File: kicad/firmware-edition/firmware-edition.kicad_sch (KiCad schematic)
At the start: 109 parts, among them J1 Solar Panel, J10 GPIO, J11 I2C-3V3, J12 GPIO, J13 SPI, J14 I2C-5V, J15 SWD, J16 Conn_01x01_Pin, J17 Conn_01x01_Pin, J18 Conn_01x01_Pin, J19 Conn_01x01_Pin, J2 BATT, J20 Conn_01x01_Pin, J21 GPIO, J3 3V3 Sensor Bus, J4 USB_C_Receptacle_USB2.0_16P, J5 Conn_01x01_Pin, J6 Conn_01x01_Pin, J7 Conn_01x01_Socket, J8 GPIO, J9 Conn_01x01_Pin, Q1 BSS84, Q2 BSS84, Q3 BSS84, SW1 BOOT_DFU, SW2 RST, U1 ADP5091, U2 TPS61023DRLR, U3 MAX-M10M-00B, U4 Si4463, U5 STM32U073KCU6, U6 TXS0102VDCTR, Y1 30MHz

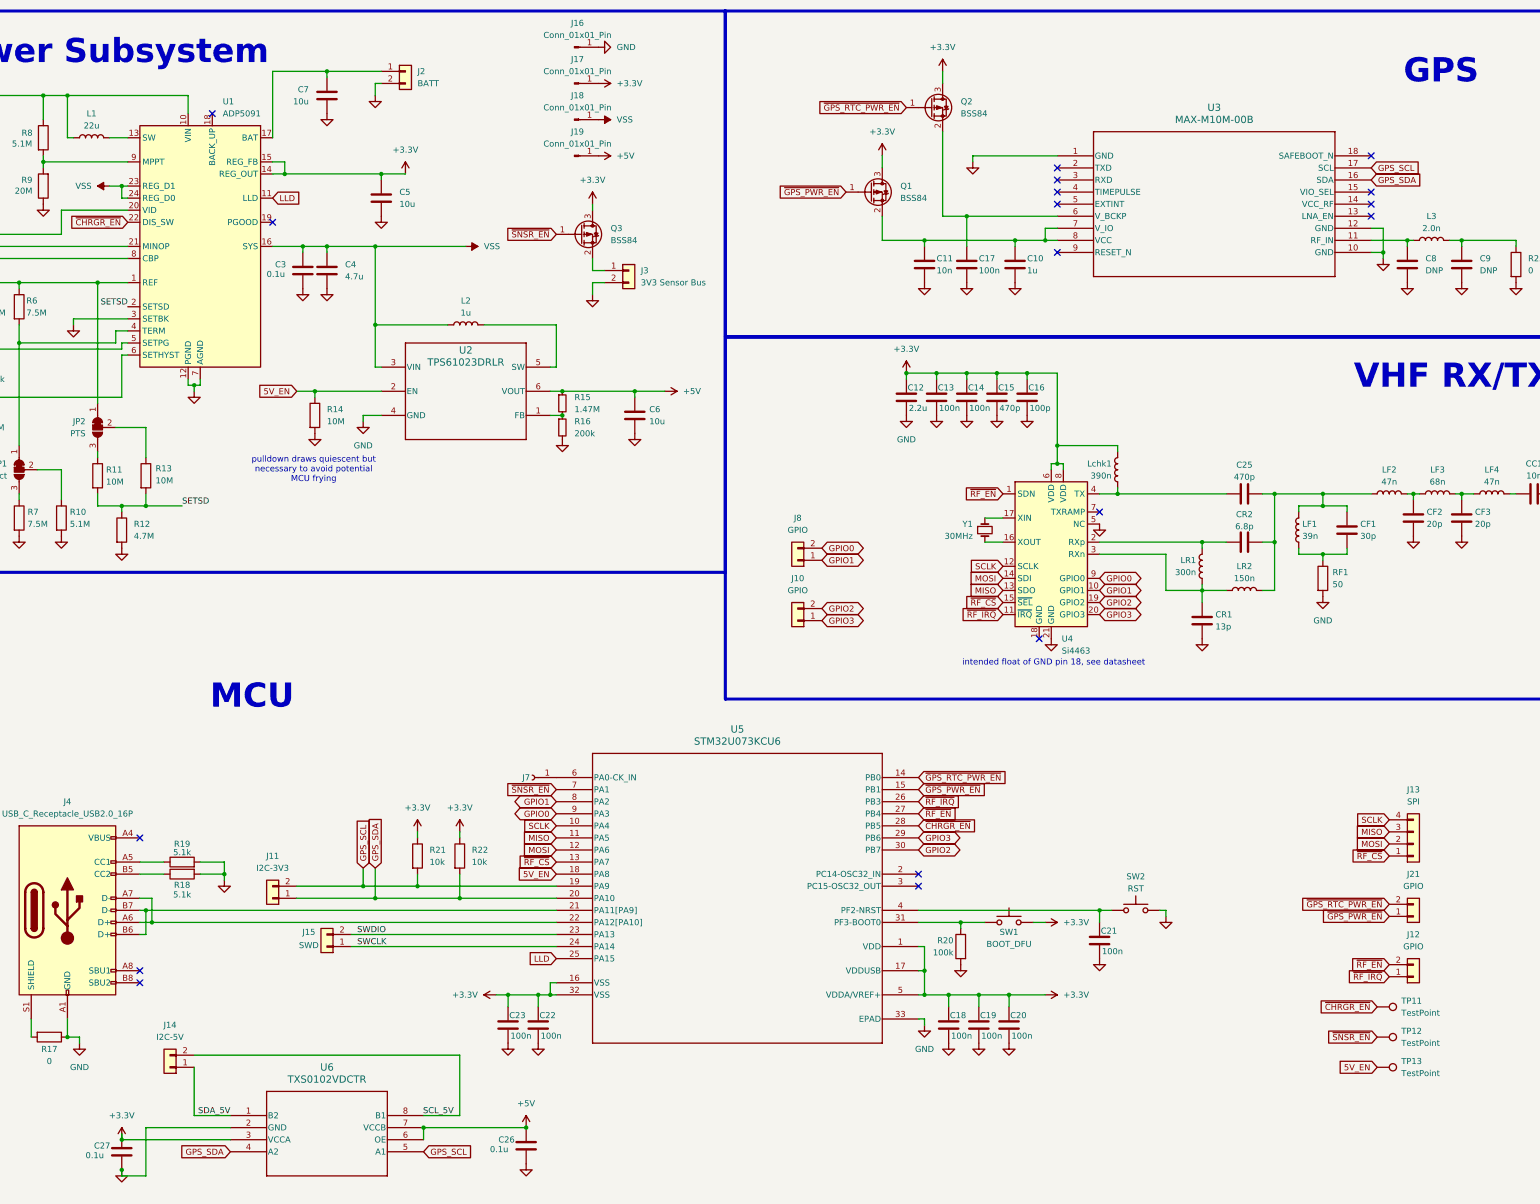
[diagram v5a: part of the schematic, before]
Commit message: improved layout, added PGOOD to MCU connection
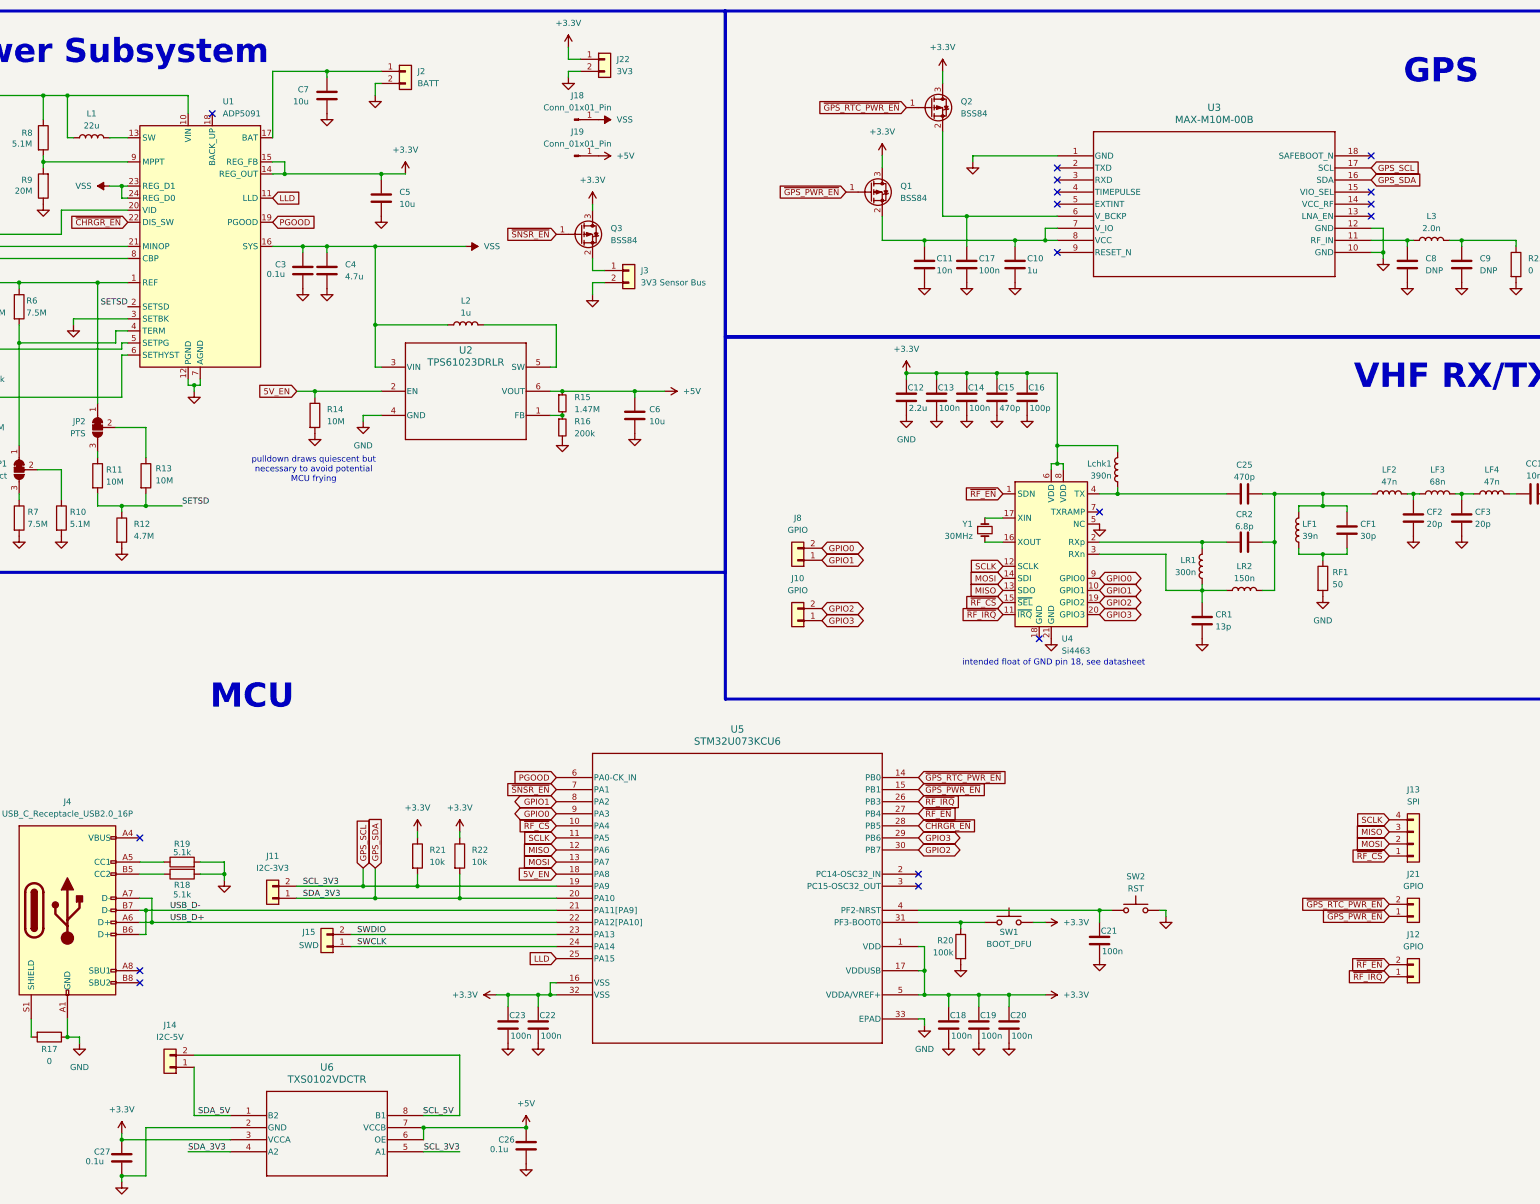
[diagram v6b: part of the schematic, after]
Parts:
- removed J16: Conn_01x01_Pin, Connector_PinHeader_2.54mm:PinHeader_1x02_P2.54mm_Vertical, symbol Connector:Conn_01x01_Pin
- removed J17: Conn_01x01_Pin, Connector_PinHeader_2.54mm:PinHeader_1x01_P2.54mm_Vertical, symbol Connector:Conn_01x01_Pin
- removed J7: Conn_01x01_Socket, Connector_PinHeader_1.00mm:PinHeader_1x01_P1.00mm_Vertical, symbol Connector:Conn_01x01_Socket
- removed TP11, TP12, TP13: TestPoint, Connector_PinHeader_1.00mm:PinHeader_1x01_P1.00mm_Vertical, symbol Connector:TestPoint
- added J22: 3V3, Connector_PinSocket_2.54mm:PinSocket_1x02_P2.54mm_Vertical, symbol Connector_Generic:Conn_01x02
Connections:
- net +3.3V: now also J22.1 (Pin_1)
- net GND: now also J22.2 (Pin_2)
- net MISO: now also U5.12 (PA6); no longer U5.11 (PA5)
- net MOSI: now also U5.13 (PA7); no longer U5.12 (PA6)
- net SCLK: now also U5.11 (PA5); no longer U5.10 (PA4)
- net ~{RF_CS}: now also U5.10 (PA4); no longer U5.13 (PA7)
- net USB_D+: now reaches J4.A6 (D+), J4.A7 (D-), U5.22 (PA12[PA10])
- net USB_D-: now reaches J4.B6 (D+), J4.B7 (D-), U5.21 (PA11[PA9])
- net PGOOD: now reaches U1.19 (PGOOD)
- net PGOOD: now also U5.6 (PA0-CK_IN)
- no-connect marks 18 -> 17
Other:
- moved on the sheet: C27

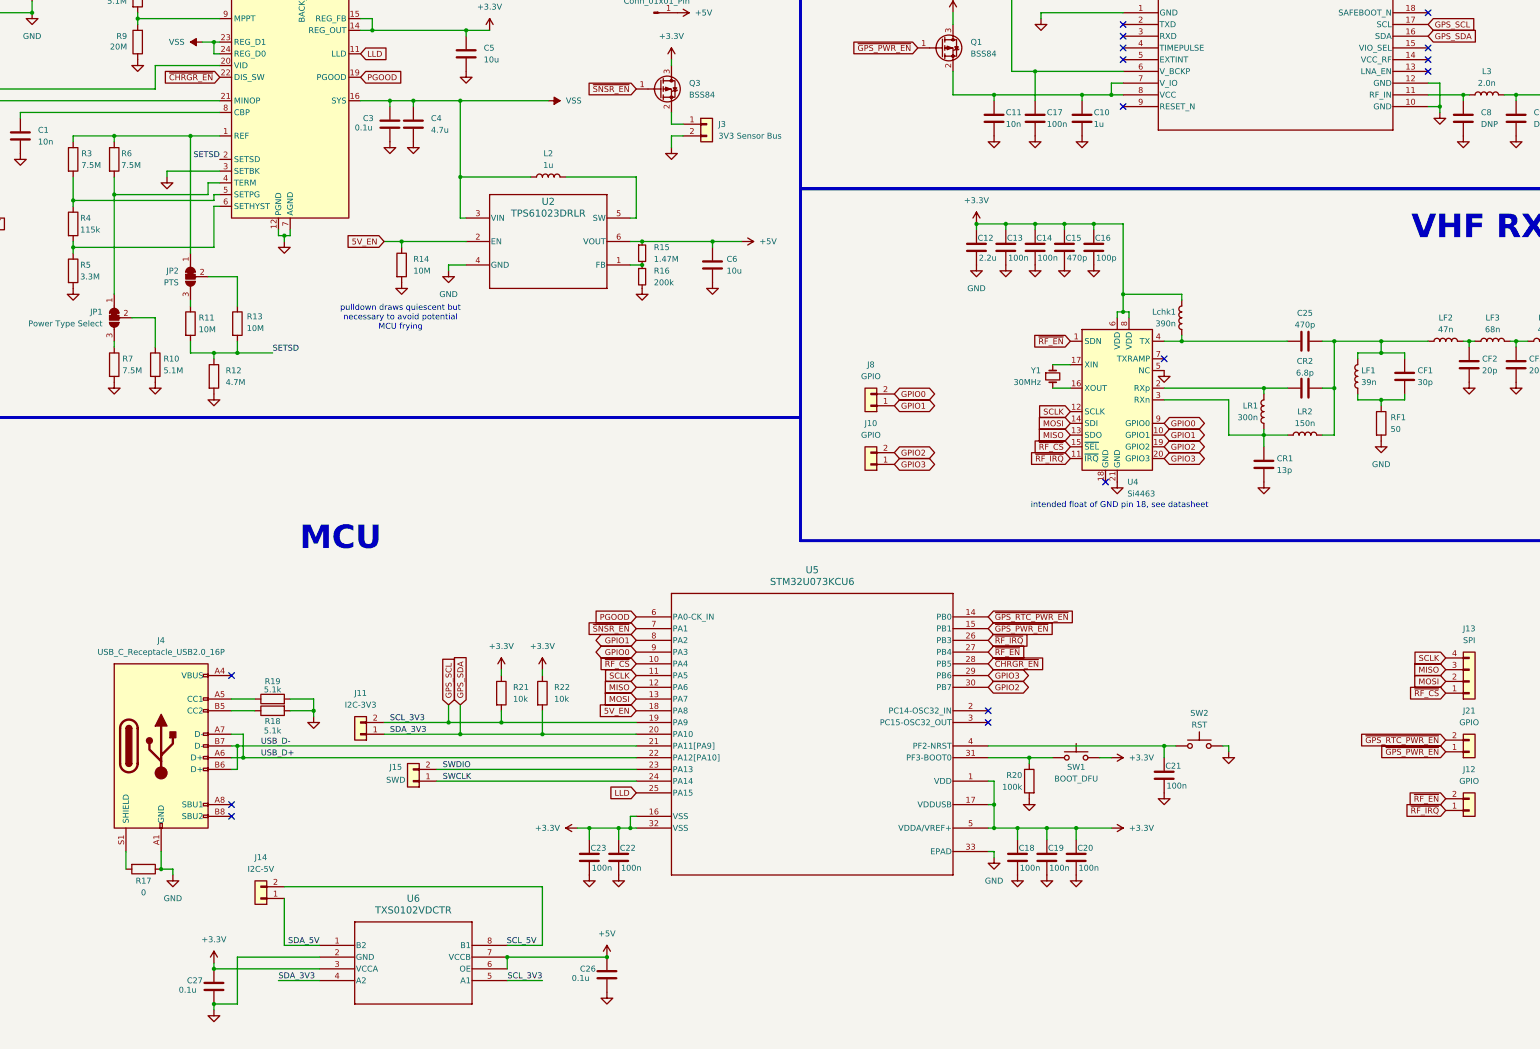
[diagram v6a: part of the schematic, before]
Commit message: Integration Board V3
Replaced USB C receptacle with Pinout for breakout board, Solved all thermal issues, VSS = GND for STM microcontroller, updated transceiver module to 0603 pads for RLC components
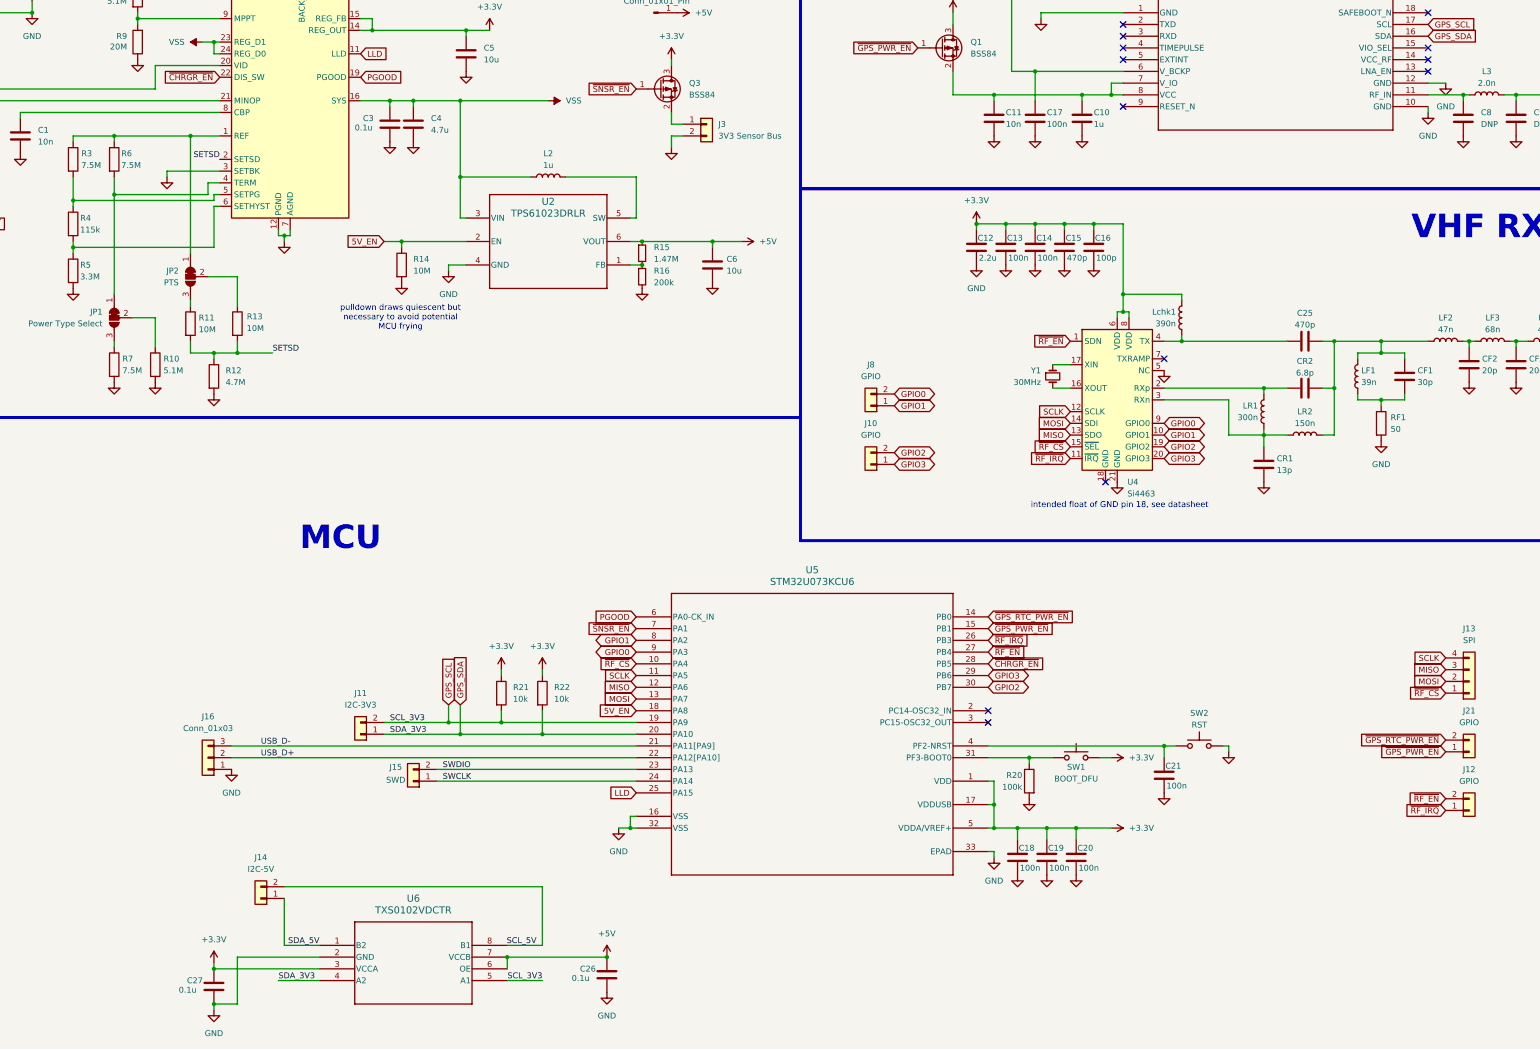
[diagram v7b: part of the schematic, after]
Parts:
- removed C22, C23: 100n, Capacitor_SMD:C_0603_1608Metric, symbol Device:C
- removed J4: USB_C_Receptacle_USB2.0_16P, Connector_USB:USB_C_Receptacle_GCT_USB4105-xx-A_16P_TopMnt_Horizontal, symbol Connector:USB_C_Receptacle_USB2.0_16P
- removed R17: 0, Resistor_SMD:R_0603_1608Metric, symbol Device:R
- removed R18, R19: 5.1k, Resistor_SMD:R_0603_1608Metric, symbol Device:R
- added J16: Conn_01x03, Connector_PinHeader_2.54mm:PinHeader_1x03_P2.54mm_Vertical, symbol Connector_Generic:Conn_01x03
- C12, C13, C14, C15, C16, C25, CC1, CF1, CF2, CF3, CR1, CR2: footprint Capacitor_SMD:C_0402_1005Metric -> Capacitor_SMD:C_0603_1608Metric
- LF1, LF2, LF3, LF4, LR1, LR2, Lchk1: footprint Inductor_SMD:L_0402_1005Metric -> Inductor_SMD:L_0603_1608Metric
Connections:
- net +3.3V: no longer U5.16 (VSS), U5.32 (VSS)
- net GND: now also U5.16 (VSS), U5.32 (VSS), J16.1 (Pin_1)
- net USB_D+: now also J16.2 (Pin_2)
- net USB_D-: now also J16.3 (Pin_3)
- no-connect marks 17 -> 14

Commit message: main board updates, stm breakout
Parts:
- removed J18, J5, J6, J9: Conn_01x01_Pin, Connector_PinHeader_2.54mm:PinHeader_1x01_P2.54mm_Vertical, symbol Connector:Conn_01x01_Pin
- added H1, H2, H3, H4: MountingHole, MountingHole:MountingHole_3.2mm_M3_ISO14580, symbol Mechanical:MountingHole
- added J4: Conn_01x04, Connector_PinHeader_2.54mm:PinHeader_1x04_P2.54mm_Vertical, symbol Connector_Generic:Conn_01x04
- added J6: Conn_01x02, Connector_PinHeader_2.54mm:PinHeader_1x02_P2.54mm_Vertical, symbol Connector_Generic:Conn_01x02
- added R17: 1M, Resistor_SMD:R_0603_1608Metric, symbol Device:R
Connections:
- net +3.3V: now also J4.1 (Pin_1)
- net 5V_EN: now also J4.4 (Pin_4)
- net GND: now also J4.3 (Pin_3), R17.1
- net LLD: now also J6.2 (Pin_2)
- net ~{CHRGR_EN}: now also R17.2
- net ~{SNSR_EN}: now also J6.1 (Pin_1)
- net VSS renamed VSYS
- net VSYS: now also J4.2 (Pin_2)
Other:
- moved on the sheet: C1, R1, R2, R8, R9
